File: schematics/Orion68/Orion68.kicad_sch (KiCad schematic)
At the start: 0 parts

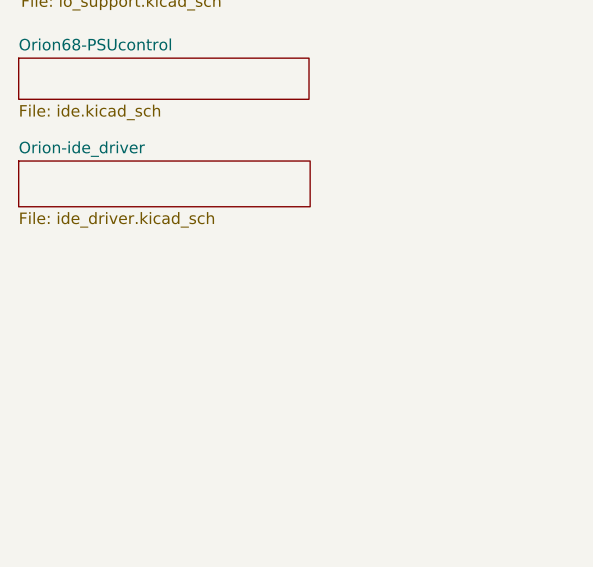
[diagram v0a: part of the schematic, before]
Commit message: 2026/10/27:(A) added A10 to pin11 74HC4078
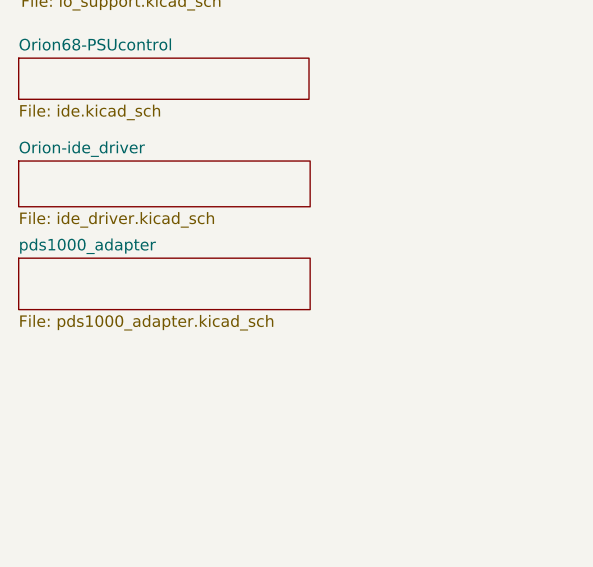
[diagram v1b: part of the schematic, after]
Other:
- added sheet pds1000_adapter (pds1000_adapter.kicad_sch)
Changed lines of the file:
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@@
+	)
+	(sheet
+		(at 19.05 137.795)
+		(size 32.385 5.715)
+		(exclude_from_sim no)
+		(in_bom yes)
+		(on_board yes)
+		(dnp no)
+		(fields_autoplaced yes)
+		(stroke
+			(width 0.1524)
+			(type solid)
+		)
+		(fill
+			(color 0 0 0 0.0000)
+		)
+		(property "Sheetname" "pds1000_adapter"
+			(at 19.05 137.0834 0)
+			(effects
+				(font
+					(size 1.27 1.27)
+				)
+				(justify left bottom)
+			)
+		)
+		(property "Sheetfile" "pds1000_adapter.kicad_sch"
+			(at 19.05 144.0946 0)
+			(effects
+				(font
+					(size 1.27 1.27)
+				)
+				(justify left top)
+			)
+		)
+		(instances
+			(project "Orion68"
+				(path "/c7ab032b-c937-44de-ab42-c91dee57f0a8"
+					(page "11")
+				)
+			)
+		)
 	)
 	(sheet
